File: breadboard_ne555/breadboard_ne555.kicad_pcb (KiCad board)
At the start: 2 copper layers, 52.1 x 11.3 mm, 12 parts, among them J1 USB_B_Micro, J2 Conn_02x02_Odd_Even, J3 Conn_02x02_Odd_Even, J4 Conn_01x05, U1 NE555

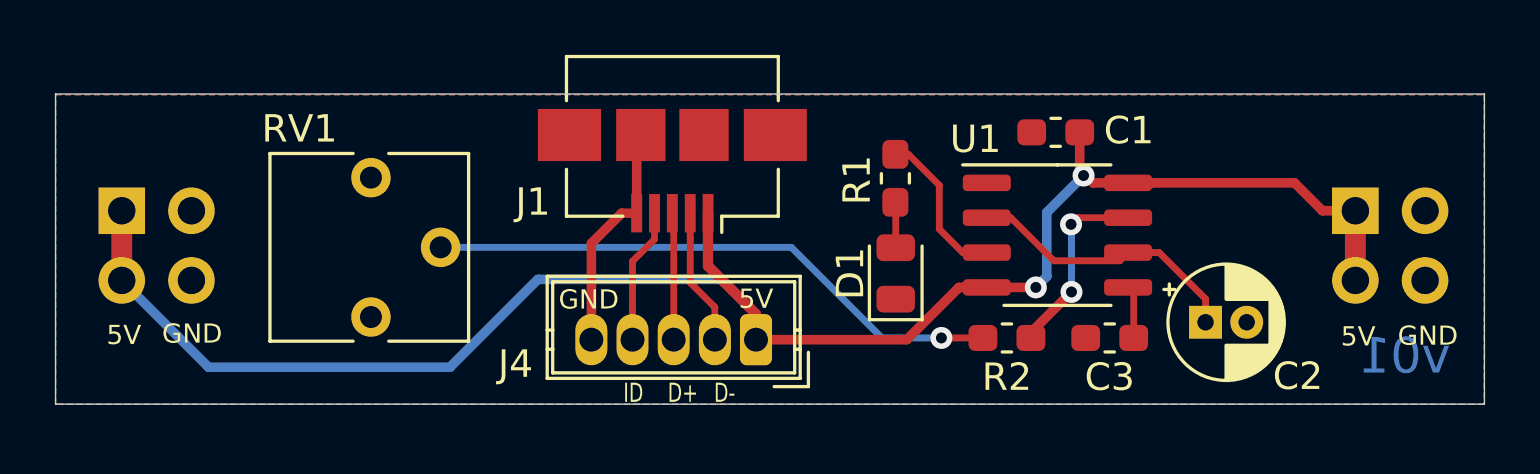
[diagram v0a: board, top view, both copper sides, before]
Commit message: update change to pcb
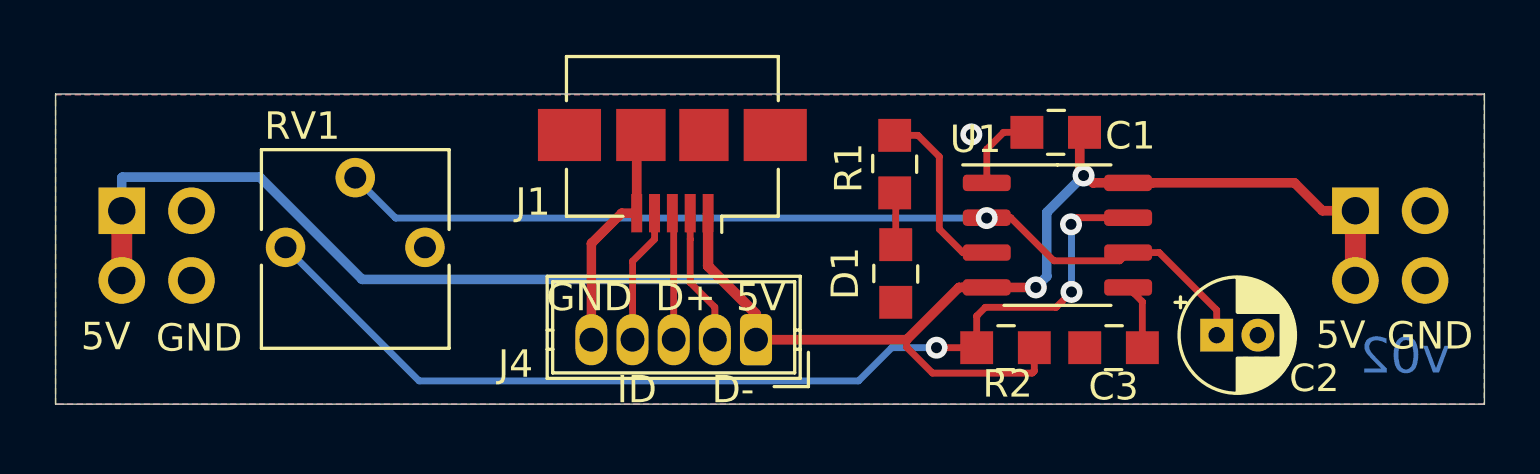
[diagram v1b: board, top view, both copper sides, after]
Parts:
- C1, C3: footprint Capacitor_SMD:C_0603_1608Metric_Pad1.05x0.95mm_HandSolder -> digikey-footprints:0805
- D1: footprint LED_SMD:LED_0805_2012Metric -> digikey-footprints:0805
- R1, R2: footprint Resistor_SMD:R_0603_1608Metric_Pad1.05x0.95mm_HandSolder -> digikey-footprints:0805
- moved RV1 3.21 mm to (119.9, 71.1), turned to 90 degrees
- moved C2 0.62 mm to (148.7, 74.3)
- moved R1 0.52 mm to (137.0, 68.1)
- moved C3 0.38 mm to (145.0, 74.8)
- moved R2 0.36 mm to (141.0, 74.8)
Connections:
- R2 pad 1: Net-(R2-Pad1) -> +5V
- RV1 pad 2: Net-(R2-Pad2) -> Net-(C2-Pad1)
- RV1 pad 3: GND -> Net-(R2-Pad2)
- U1 pad 7: Net-(R2-Pad1) -> Net-(R2-Pad2)
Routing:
- net Net-(C2-Pad1): track 10.3 -> 34.6 mm, vias 0 -> 1
- net Net-(R2-Pad2): track 21.1 -> 37.3 mm, vias 1 -> 3
- net Net-(R2-Pad1): track 6.94 -> 0.00 mm, vias 2 -> 0
- net +5V: track 65.4 -> 71.7 mm
- net GND: track 8.53 -> 11.5 mm, vias 0 -> 1
- net Net-(R1-Pad1): track 5.75 -> 6.67 mm
- net Net-(C3-Pad1): track 1.93 -> 2.70 mm
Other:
- board text added: "breadboard power & 555 timer shane 2020/11/15"
- board text added: "v02"
- board text removed: "breadboard power & 555 timer shane 2020/11/07"
- board text removed: "v01"
